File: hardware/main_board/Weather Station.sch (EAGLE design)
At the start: 34 parts, among them J2 RJ12, Q1 200mA/40V, Q2 220mA/50V/3.5Ω, U1 328P, U2 MCP1703T-3302E/CB, U3 W25X40CLSNIG, X2 B2B-PH-K-S, X3 B2B-XH-2, Y1 8MHz

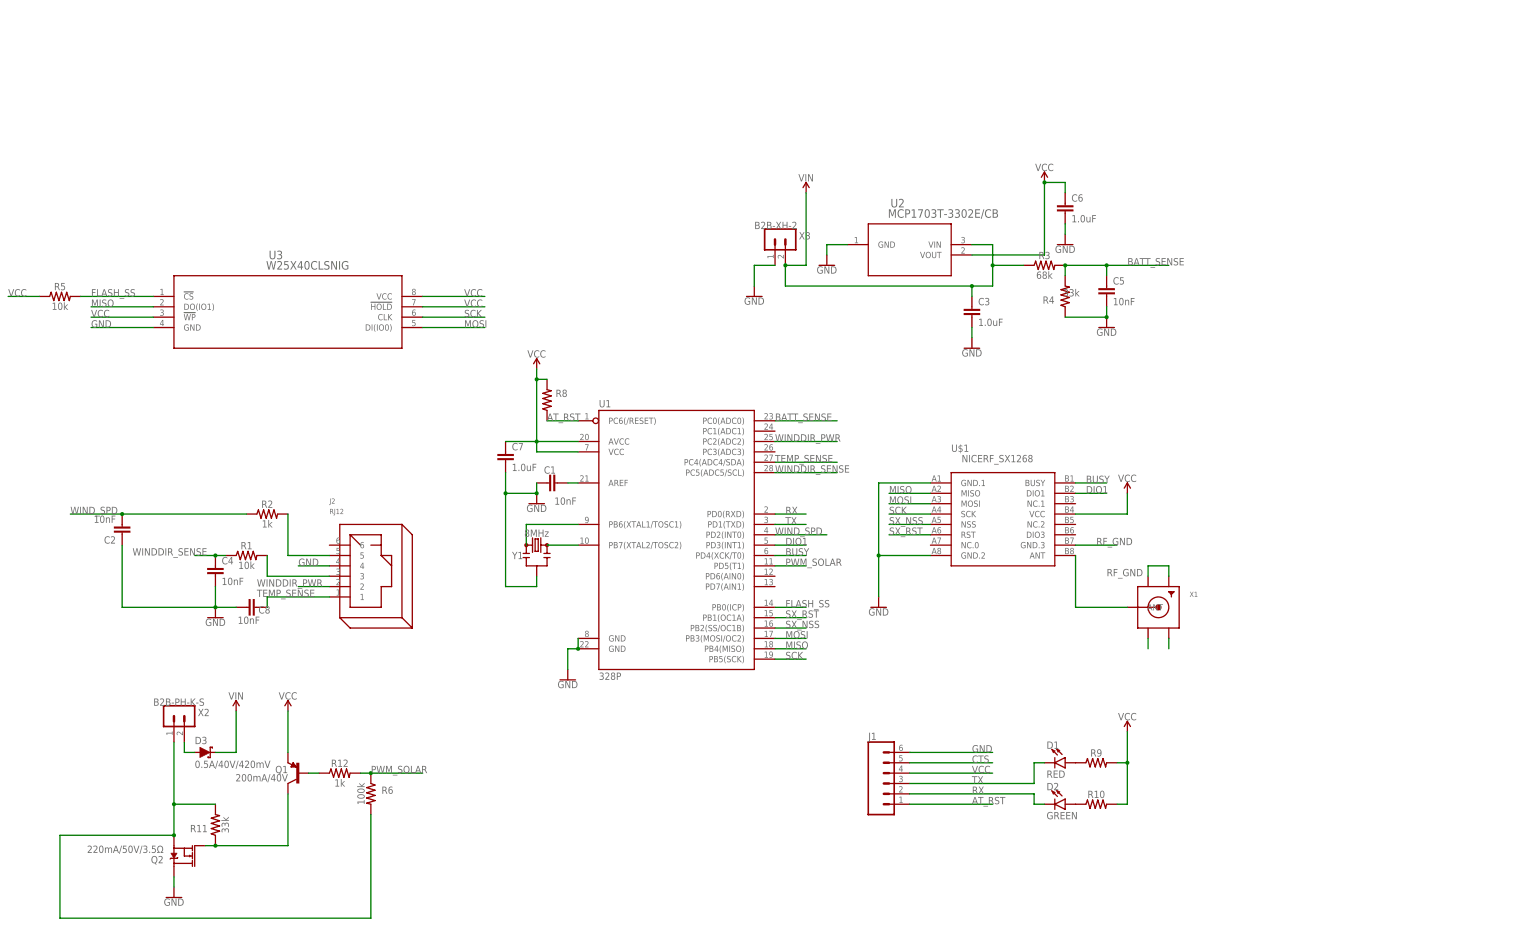
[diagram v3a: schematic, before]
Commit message: Added stationID to EEPROM and made changeable. Some hardware work.
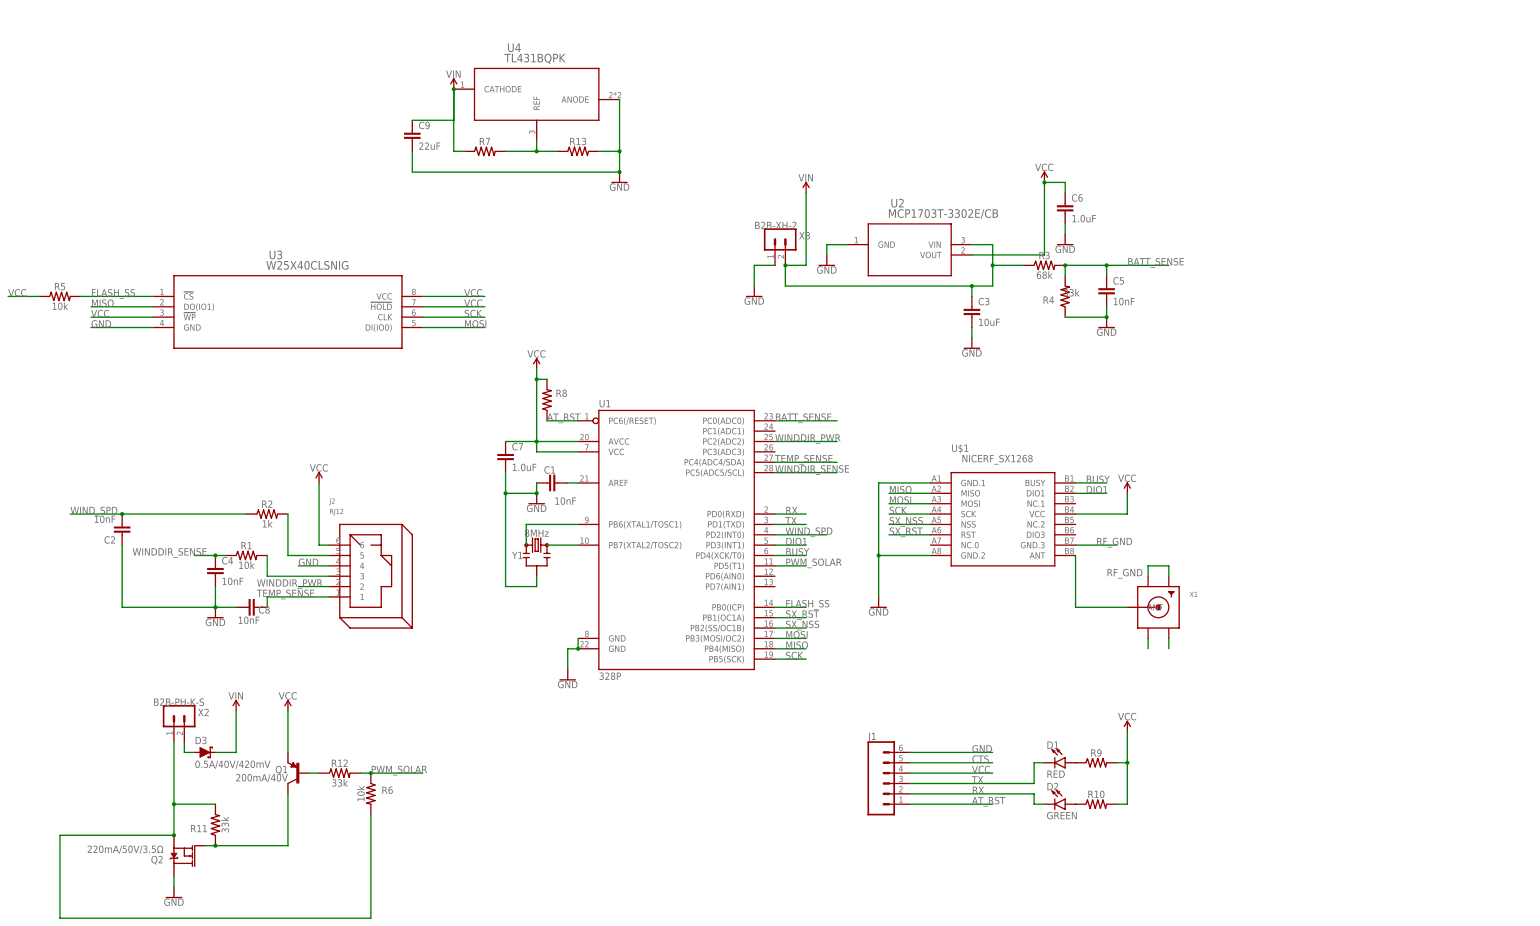
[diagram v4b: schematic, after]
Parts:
- added C9: 22uF, SparkFun-Capacitors:22UF-0805-6.3V-20%
- added R13, R7: (no value), SparkFun-Resistors:RESISTOR0805
- added U4: TL431BQPK, my-components:TL431BQPK
- C3: value 1.0uF -> 10uF
- R12: value 1k -> 33k
- R6: value 100k -> 10k
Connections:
- new net N$1: R13.1, R7.2, U4.REF
- net GND: now also C9.2, R13.2, U4.ANODE
- net VCC: now also J2.6
- net VIN: now also C9.1, R7.1, U4.CATHODE
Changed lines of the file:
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@@
 <part name="R4" library="SparkFun-Resistors" library_urn="urn:adsk.eagle:library:532" deviceset="RESISTOR" device="0805" package3d_urn="urn:adsk.eagle:package:39651/1" value="33k"/>
 <part name="C1" library="SparkFun-Capacitors" library_urn="urn:adsk.eagle:library:510" deviceset="10NF" device="-0603-50V-10%" package3d_urn="urn:adsk.eagle:package:37414/1" value="10nF"/>
-<part name="C3" library="SparkFun-Capacitors" library_urn="urn:adsk.eagle:library:510" deviceset="1.0UF" device="-0603-16V-10%" package3d_urn="urn:adsk.eagle:package:37414/1" value="1.0uF"/>
+<part name="C3" library="SparkFun-Capacitors" library_urn="urn:adsk.eagle:library:510" deviceset="1.0UF" device="-0603-16V-10%" package3d_urn="urn:adsk.eagle:package:37414/1" value="10uF"/>
 <part name="C6" library="SparkFun-Capacitors" library_urn="urn:adsk.eagle:library:510" deviceset="1.0UF" device="-0603-16V-10%" package3d_urn="urn:adsk.eagle:package:37414/1" value="1.0uF"/>
 <part name="GND8" library="SparkFun-PowerSymbols" library_urn="urn:adsk.eagle:library:530" deviceset="GND" device=""/>
@@
 <part name="Q2" library="SparkFun-DiscreteSemi" library_urn="urn:adsk.eagle:library:514" deviceset="MOSFET-NCH" device="-BSS138" package3d_urn="urn:adsk.eagle:package:38446/1" value="220mA/50V/3.5Ω"/>
 <part name="R11" library="SparkFun-Resistors" library_urn="urn:adsk.eagle:library:532" deviceset="RESISTOR" device="0805" package3d_urn="urn:adsk.eagle:package:39651/1" value="33k"/>
-<part name="R12" library="SparkFun-Resistors" library_urn="urn:adsk.eagle:library:532" deviceset="RESISTOR" device="0805" package3d_urn="urn:adsk.eagle:package:39651/1" value="1k"/>
+<part name="R12" library="SparkFun-Resistors" library_urn="urn:adsk.eagle:library:532" deviceset="RESISTOR" device="0805" package3d_urn="urn:adsk.eagle:package:39651/1" value="33k"/>
 <part name="SUPPLY5" library="SparkFun-PowerSymbols" library_urn="urn:adsk.eagle:library:530" deviceset="VIN" device=""/>
 <part name="SUPPLY7" library="SparkFun-PowerSymbols" library_urn="urn:adsk.eagle:library:530" deviceset="VIN" device=""/>
 <part name="SUPPLY8" library="SparkFun-PowerSymbols" library_urn="urn:adsk.eagle:library:530" deviceset="VCC" device=""/>
 <part name="D3" library="SparkFun-DiscreteSemi" library_urn="urn:adsk.eagle:library:514" deviceset="DIODE-SCHOTTKY" device="-PMEG4005EJ" package3d_urn="urn:adsk.eagle:package:38441/1" value="0.5A/40V/420mV"/>
-<part name="R6" library="SparkFun-Resistors" library_urn="urn:adsk.eagle:library:532" deviceset="RESISTOR" device="0805" package3d_urn="urn:adsk.eagle:package:39651/1" value="100k"/>
+<part name="R6" library="SparkFun-Resistors" library_urn="urn:adsk.eagle:library:532" deviceset="RESISTOR" device="0805" package3d_urn="urn:adsk.eagle:package:39651/1" value="10k"/>
+<part name="GND11" library="SparkFun-PowerSymbols" library_urn="urn:adsk.eagle:library:530" deviceset="GND" device=""/>
+<part name="U4" library="my-components" deviceset="TL431BQPK" device=""/>
+<part name="SUPPLY4" library="SparkFun-PowerSymbols" library_urn="urn:adsk.eagle:library:530" deviceset="VIN" device=""/>
+<part name="R7" library="SparkFun-Resistors" library_urn="urn:adsk.eagle:library:532" deviceset="RESISTOR" device="0805" package3d_urn="urn:adsk.eagle:package:39651/1" value=" "/>
+<part name="R13" library="SparkFun-Resistors" library_urn="urn:adsk.eagle:library:532" deviceset="RESISTOR" device="0805" package3d_urn="urn:adsk.eagle:package:39651/1" value=" "/>
+<part name="C9" library="SparkFun-Capacitors" library_urn="urn:adsk.eagle:library:510" deviceset="22UF" device="-0805-6.3V-20%" package3d_urn="urn:adsk.eagle:package:37429/1" value="22uF"/>
+<part name="SUPPLY9" library="SparkFun-PowerSymbols" library_urn="urn:adsk.eagle:library:530" deviceset="VCC" device=""/>
 </parts>
 <sheets>
@@
 <attribute name="NAME" x="-34.036" y="-25.4" size="1.778" layer="95" font="vector" align="bottom-center"/>
 <attribute name="VALUE" x="-39.624" y="-25.4" size="1.778" layer="96" font="vector" rot="R270" align="top-center"/>
+</instance>
+<instance part="GND11" gate="1" x="22.86" y="124.46" smashed="yes">
+<attribute name="VALUE" x="22.86" y="124.206" size="1.778" layer="96" align="top-center"/>
+</instance>
+<instance part="U4" gate="A" x="-20.32" y="147.32" smashed="yes">
+<attribute name="NAME" x="-4.7244" y="156.4386" size="2.0828" layer="95" ratio="6" rot="SR0"/>
+<attribute name="VALUE" x="-5.3594" y="153.8986" size="2.0828" layer="96" ratio="6" rot="SR0"/>
+</instance>
+<instance part="SUPPLY4" gate="G$1" x="-17.78" y="147.32" smashed="yes">
+<attribute name="VALUE" x="-17.78" y="150.114" size="1.778" layer="96" align="bottom-center"/>
+</instance>
+<instance part="R7" gate="G$1" x="-10.16" y="132.08" smashed="yes">
+<attribute name="NAME" x="-10.16" y="133.604" size="1.778" layer="95" font="vector" align="bottom-center"/>
+<attribute name="VALUE" x="-10.16" y="130.556" size="1.778" layer="96" font="vector" align="top-center"/>
+</instance>
+<instance part="R13" gate="G$1" x="12.7" y="132.08" smashed="yes">
+<attribute name="NAME" x="12.7" y="133.604" size="1.778" layer="95" font="vector" align="bottom-center"/>
+<attribute name="VALUE" x="12.7" y="130.556" size="1.778" layer="96" font="vector" align="top-center"/>
+</instance>
+<instance part="C9" gate="G$1" x="-27.94" y="134.62" smashed="yes">
+<attribute name="NAME" x="-26.416" y="137.541" size="1.778" layer="95" font="vector"/>
+<attribute name="VALUE" x="-26.416" y="132.461" size="1.778" layer="96" font="vector"/>
+</instance>
+<instance part="SUPPLY9" gate="G$1" x="-50.8" y="50.8" smashed="yes">
+<attribute name="VALUE" x="-50.8" y="53.594" size="1.778" layer="96" align="bottom-center"/>
 </instance>
 </instances>
@@
 <pinref part="GND10" gate="1" pin="GND"/>
 <wire x1="-86.36" y1="-45.72" x2="-86.36" y2="-48.26" width="0.1524" layer="91"/>
+</segment>
+<segment>
+<pinref part="U4" gate="A" pin="ANODE"/>
+<pinref part="GND11" gate="1" pin="GND"/>
+<wire x1="22.86" y1="127" x2="22.86" y2="132.08" width="0.1524" layer="91"/>
+<pinref part="R13" gate="G$1" pin="2"/>
+<wire x1="22.86" y1="132.08" x2="22.86" y2="144.78" width="0.1524" layer="91"/>
+<wire x1="17.78" y1="132.08" x2="22.86" y2="132.08" width="0.1524" layer="91"/>
+<junction x="22.86" y="132.08"/>
+<pinref part="C9" gate="G$1" pin="2"/>
+<wire x1="-27.94" y1="132.08" x2="-27.94" y2="127" width="0.1524" layer="91"/>
+<wire x1="-27.94" y1="127" x2="22.86" y2="127" width="0.1524" layer="91"/>
+<junction x="22.86" y="127"/>
 </segment>
 </net>
@@
 <wire x1="-58.42" y1="-15.24" x2="-58.42" y2="-5.08" width="0.1524" layer="91"/>
 </segment>
+<segment>
+<pinref part="J2" gate="G$1" pin="6"/>
+<pinref part="SUPPLY9" gate="G$1" pin="VCC"/>
+<wire x1="-48.26" y1="35.56" x2="-50.8" y2="35.56" width="0.1524" layer="91"/>
+<wire x1="-50.8" y1="35.56" x2="-50.8" y2="50.8" width="0.1524" layer="91"/>
+</segment>
 </net>
 <net name="MISO" class="0">
@@
 <pinref part="U1" gate="G$1" pin="PD2(INT0)"/>
 <wire x1="60.96" y1="38.1" x2="73.66" y2="38.1" width="0.1524" layer="91"/>
-<label x="60.96" y="38.1" size="1.778" layer="95"/>
+<label x="63.5" y="38.1" size="1.778" layer="95"/>
 </segment>
 <segment>
@@
 <wire x1="-71.12" y1="-15.24" x2="-71.12" y2="-5.08" width="0.1524" layer="91"/>
 </segment>
+<segment>
+<pinref part="U4" gate="A" pin="CATHODE"/>
+<pinref part="SUPPLY4" gate="G$1" pin="VIN"/>
+<pinref part="R7" gate="G$1" pin="1"/>
+<wire x1="-17.78" y1="147.32" x2="-17.78" y2="132.08" width="0.1524" layer="91"/>
+<wire x1="-17.78" y1="132.08" x2="-15.24" y2="132.08" width="0.1524" layer="91"/>
+<junction x="-17.78" y="147.32"/>
+<pinref part="C9" gate="G$1" pin="1"/>
+<wire x1="-17.78" y1="147.32" x2="-17.78" y2="139.7" width="0.1524" layer="91"/>
+<wire x1="-17.78" y1="139.7" x2="-27.94" y2="139.7" width="0.1524" layer="91"/>
+</segment>
 </net>
 <net name="PWM_SOLAR" class="0">
@@
 </segment>
 </net>
+<net name="N$1" class="0">
+<segment>
+<pinref part="R13" gate="G$1" pin="1"/>
+<pinref part="R7" gate="G$1" pin="2"/>
+<wire x1="7.62" y1="132.08" x2="2.54" y2="132.08" width="0.1524" layer="91"/>
+<pinref part="U4" gate="A" pin="REF"/>
+<wire x1="2.54" y1="132.08" x2="-5.08" y2="132.08" width="0.1524" layer="91"/>
+<wire x1="2.54" y1="134.62" x2="2.54" y2="132.08" width="0.1524" layer="91"/>
+<junction x="2.54" y="132.08"/>
+</segment>
+</net>

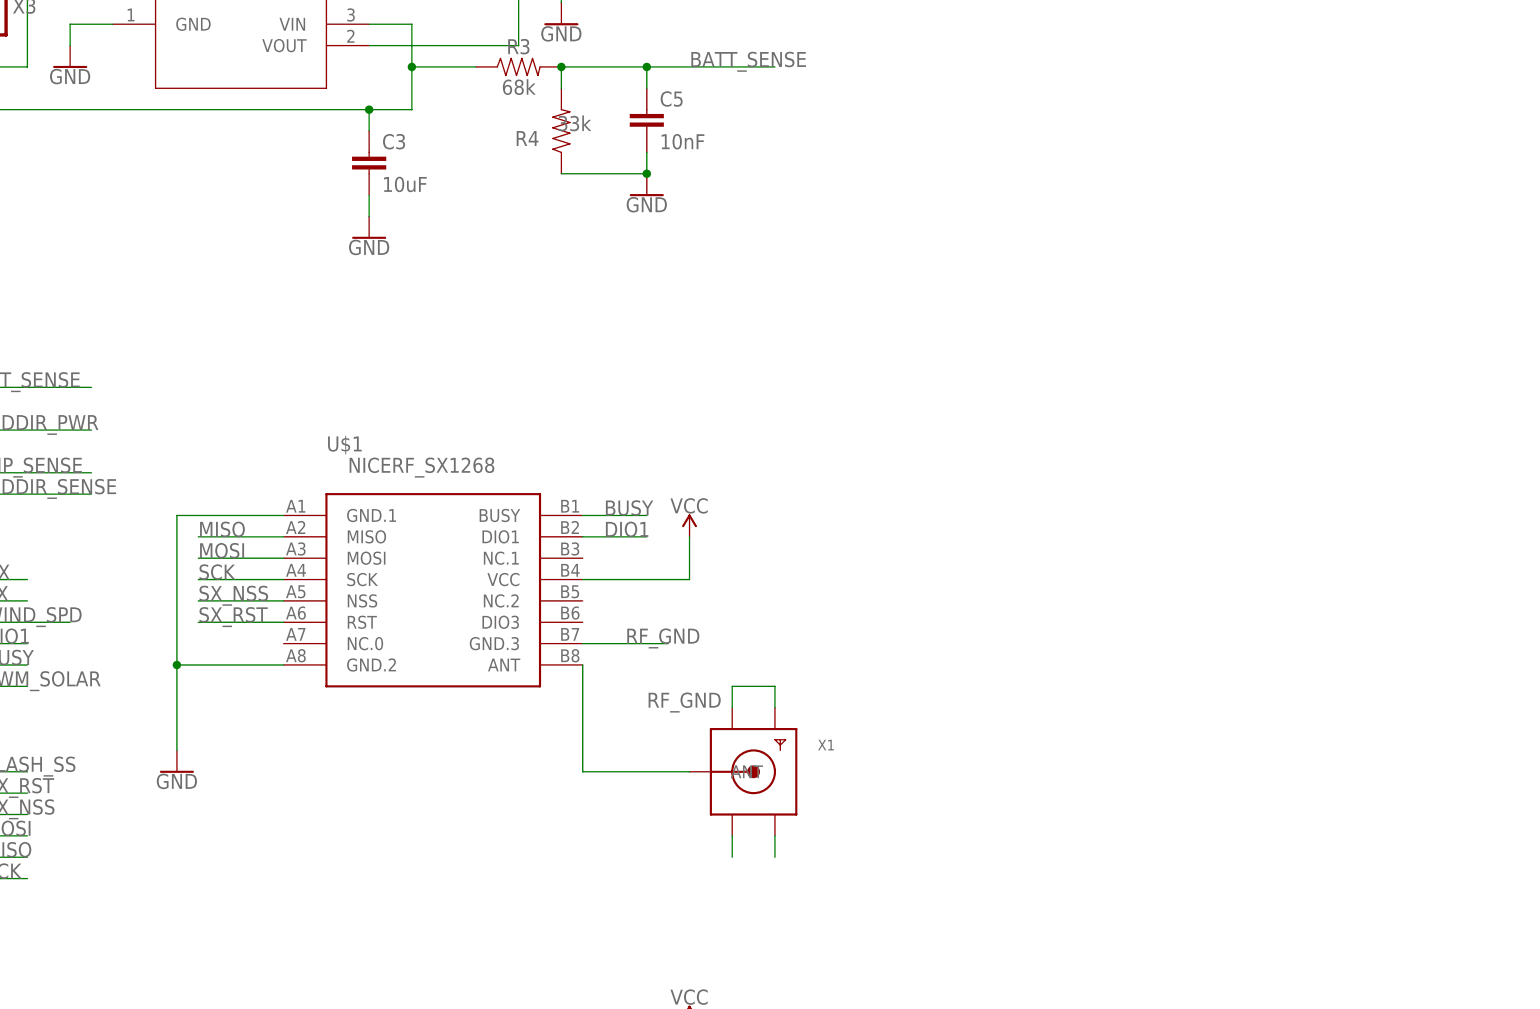
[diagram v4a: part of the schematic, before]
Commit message: Switched to DRF126xT module
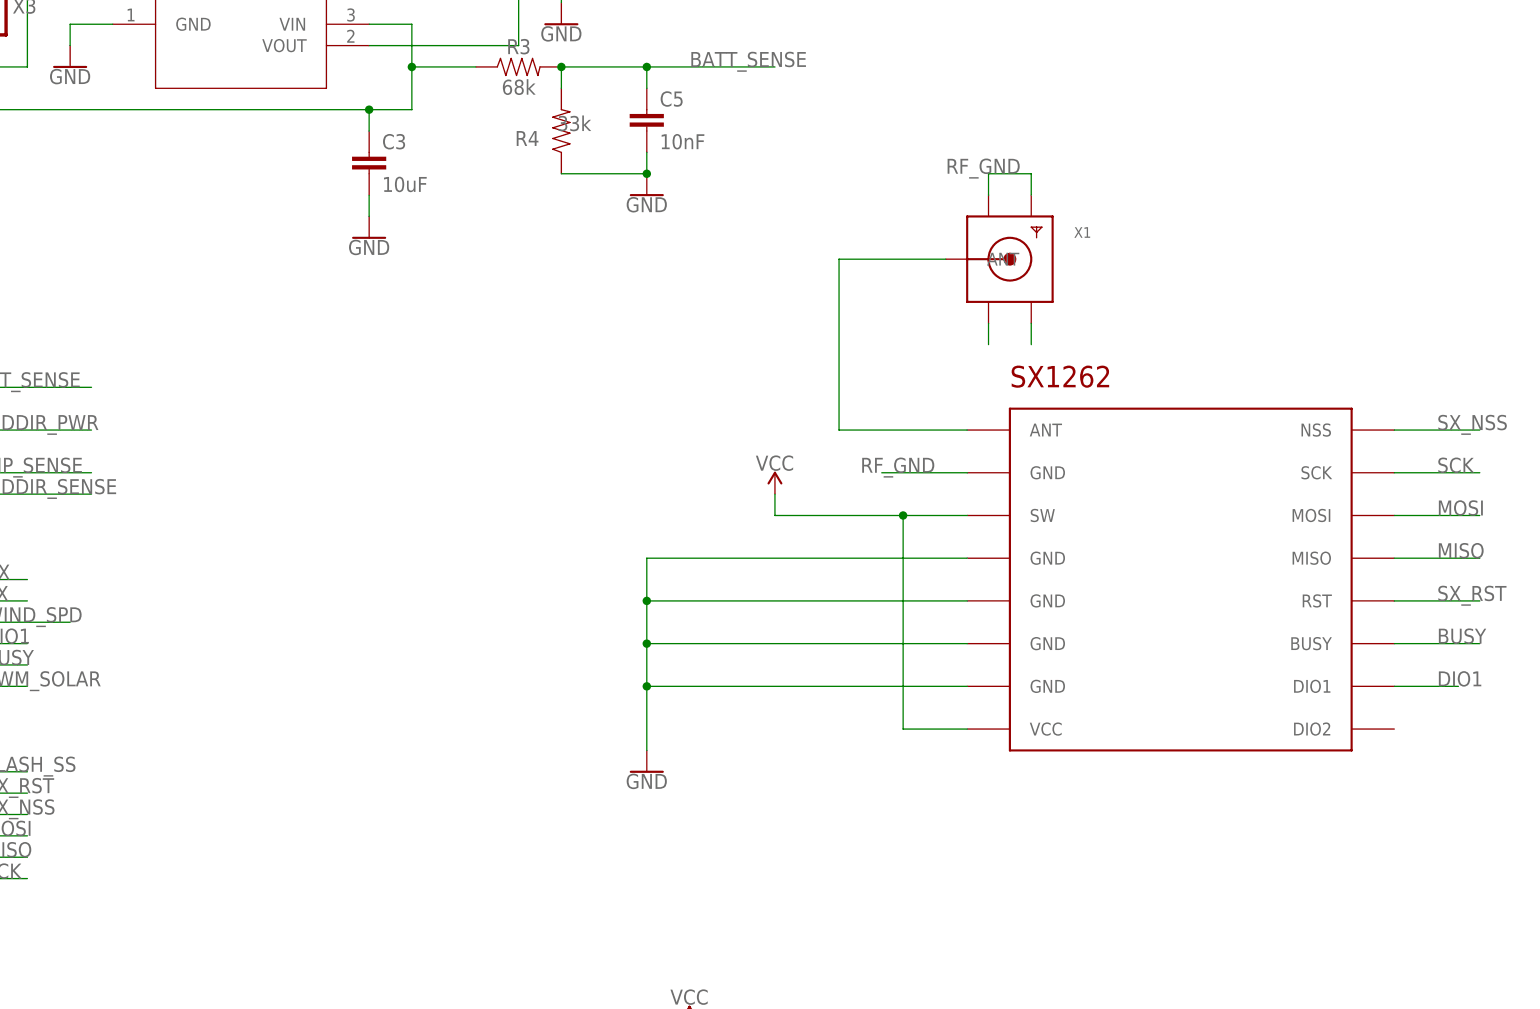
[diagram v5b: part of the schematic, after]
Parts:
- U$1: value NICERF_SX1268 -> SX1262; device diy-modules:WIRELESS-LORA-NICERF1268 -> RadioShield:SX1262
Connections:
- net GND: now also U$1.GND@2, U$1.GND@3, U$1.GND@4, U$1.GND@5; no longer U$1.GND.1, U$1.GND.2
- net RF_GND: now also U$1.GND@1; no longer U$1.GND.3
- net VCC: now also U$1.SW
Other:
- moved on the sheet: X1
